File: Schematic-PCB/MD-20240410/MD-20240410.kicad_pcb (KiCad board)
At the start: 2 copper layers, 100.5 x 56.4 mm, 0 parts

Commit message: MD基板へ部品を仮で配置
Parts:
- added C1: 22n, Capacitor_SMD:C_0603_1608Metric, F.Cu at (147.8, 76.2)
- added C10: 220n, Capacitor_SMD:C_0603_1608Metric, F.Cu at (152.0, 76.2)
- added C11: 22n, Capacitor_SMD:C_0603_1608Metric, F.Cu at (147.8, 96.0)
- added C12: 220n, Capacitor_SMD:C_0603_1608Metric, F.Cu at (147.8, 99.0)
- added C13: 22n, Capacitor_SMD:C_0603_1608Metric, F.Cu at (152.2, 99.0)
- added C14: 220n, Capacitor_SMD:C_0603_1608Metric, F.Cu at (152.2, 96.0)
- added C2: 220n, Capacitor_SMD:C_0603_1608Metric, F.Cu at (147.8, 79.2)
- added C3: 4.7u, Capacitor_SMD:C_0603_1608Metric, F.Cu at (153.5, 87.5)
- added C4: 4.7u, Capacitor_SMD:C_0603_1608Metric, F.Cu at (155.0, 87.5)
- added C5: 50u, Capacitor_SMD:C_0603_1608Metric, F.Cu at (156.5, 87.5)
- added C7: 0.1u, Capacitor_SMD:C_0603_1608Metric, F.Cu at (158.0, 87.5)
- added C8: 0.1u, Capacitor_SMD:C_0603_1608Metric, F.Cu at (159.5, 87.5)
- added C9: 22n, Capacitor_SMD:C_0603_1608Metric, F.Cu at (152.0, 79.2)
- added D1: LED, LED_SMD:LED_0805_2012Metric, B.Cu at (168.5, 87.5)
- added D2: 16.2V, Diode_SMD:D_SOD-323, F.Cu at (136.8, 87.5)
- added J1: Conn_01x05_Pin, Connector_FFC-FPC:TE_84953-5_1x05-1MP_P1.0mm_Horizontal, F.Cu at (120.8, 87.5)
- added J2: Conn_01x05_Pin, Connector_FFC-FPC:TE_84953-5_1x05-1MP_P1.0mm_Horizontal, F.Cu at (179.2, 87.5)
- added J3: Conn_01x02_Pin, Connector_JST:JST_VH_B2P-VH_1x02_P3.96mm_Vertical, F.Cu at (130.8, 75.5)
- added J4: Conn_01x02_Pin, Connector_JST:JST_VH_B2P-VH_1x02_P3.96mm_Vertical, F.Cu at (169.0, 79.5)
- added J5: Conn_01x02_Pin, Connector_JST:JST_VH_B2P-VH_1x02_P3.96mm_Vertical, F.Cu at (130.8, 95.5)
- added J6: Conn_01x02_Pin, Connector_JST:JST_VH_B2P-VH_1x02_P3.96mm_Vertical, F.Cu at (169.2, 99.5)
- added J7: Conn_01x02_Pin, Connector_JST:JST_VH_B2P-VH_1x02_P3.96mm_Vertical, F.Cu at (130.8, 85.5)
- added Q2: PMOS, Package_TO_SOT_SMD:TO-252-2, F.Cu at (145.0, 87.5)
- added R1: 330, Resistor_SMD:R_0603_1608Metric, F.Cu at (165.8, 87.5)
- added R10: NP, Resistor_SMD:R_0603_1608Metric, F.Cu at (163.0, 78.5)
- added R11: 20k, Resistor_SMD:R_0603_1608Metric, F.Cu at (163.0, 75.5)
- added R12: 2.49k, Resistor_SMD:R_0603_1608Metric, F.Cu at (136.8, 98.2)
- added R13: 10k, Resistor_SMD:R_0603_1608Metric, F.Cu at (136.8, 95.2)
- added R14: NP, Resistor_SMD:R_0603_1608Metric, F.Cu at (136.8, 96.8)
- added R15: 20k, Resistor_SMD:R_0603_1608Metric, F.Cu at (136.8, 99.8)
- added R16: 2.49k, Resistor_SMD:R_0603_1608Metric, F.Cu at (163.2, 96.8)
- added R17: 10k, Resistor_SMD:R_0603_1608Metric, F.Cu at (163.2, 99.8)
- added R18: NP, Resistor_SMD:R_0603_1608Metric, F.Cu at (163.2, 98.2)
- added R19: 20k, Resistor_SMD:R_0603_1608Metric, F.Cu at (163.2, 95.2)
- added R3: 10k, Resistor_SMD:R_0603_1608Metric, F.Cu at (136.8, 75.5)
- added R4: 2.49k, Resistor_SMD:R_0603_1608Metric, F.Cu at (136.8, 78.5)
- added R5: 100k, Resistor_SMD:R_0603_1608Metric, F.Cu at (152.0, 87.5)
- added R6: NP, Resistor_SMD:R_0603_1608Metric, F.Cu at (136.8, 77.0)
- added R7: 20k, Resistor_SMD:R_0603_1608Metric, F.Cu at (136.8, 80.0)
- added R8: 2.49k, Resistor_SMD:R_0603_1608Metric, F.Cu at (163.0, 77.0)
- added R9: 10k, Resistor_SMD:R_0603_1608Metric, F.Cu at (163.0, 80.0)
- added U1: ~, Package_SO:HTSSOP-16-1EP_4.4x5mm_P0.65mm_EP3.4x5mm_Mask2.46x2.31mm_ThermalVias, F.Cu at (142.6, 77.7)
- added U2: ~, Package_SO:HTSSOP-16-1EP_4.4x5mm_P0.65mm_EP3.4x5mm_Mask2.46x2.31mm_ThermalVias, F.Cu at (157.1, 77.6)
- added U3: ~, Package_SO:HTSSOP-16-1EP_4.4x5mm_P0.65mm_EP3.4x5mm_Mask2.46x2.31mm_ThermalVias, F.Cu at (142.6, 97.5)
- added U4: ~, Package_SO:HTSSOP-16-1EP_4.4x5mm_P0.65mm_EP3.4x5mm_Mask2.46x2.31mm_ThermalVias, F.Cu at (157.4, 97.5)

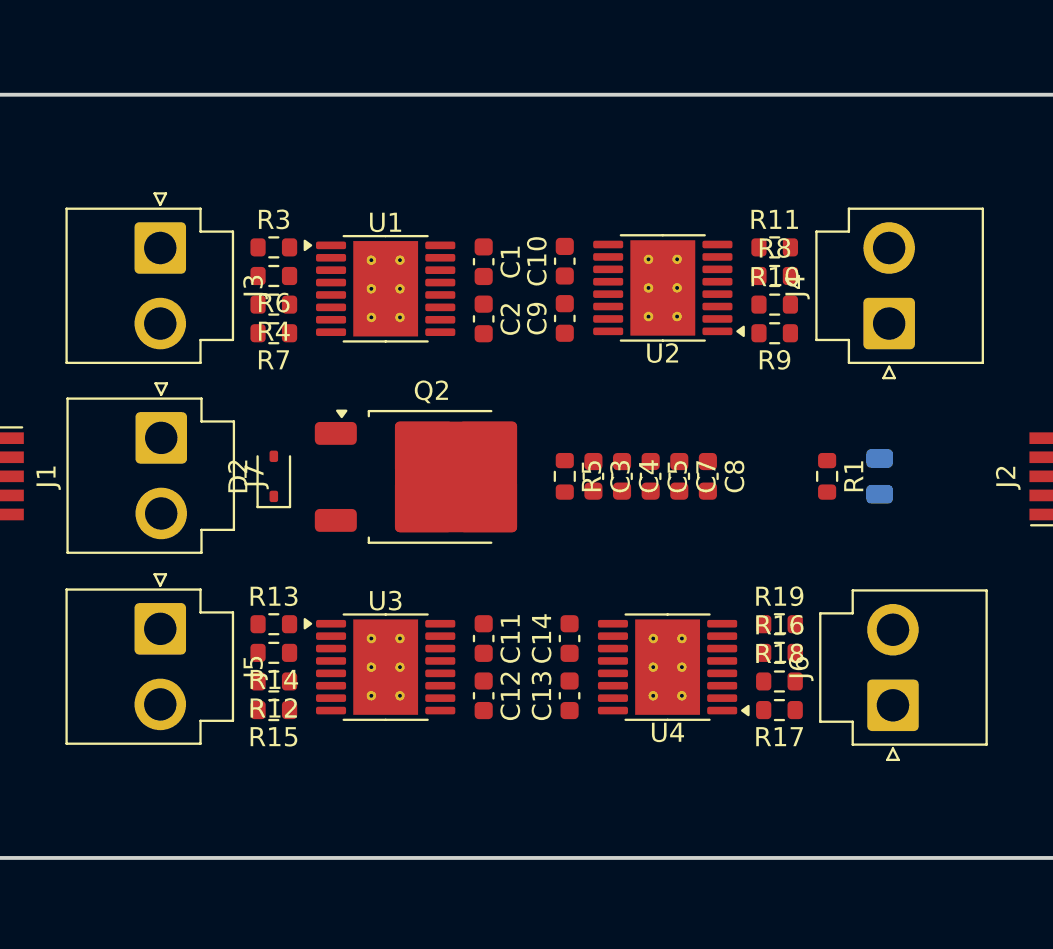
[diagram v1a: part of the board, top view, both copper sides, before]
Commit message: MD基板のPCBを更新
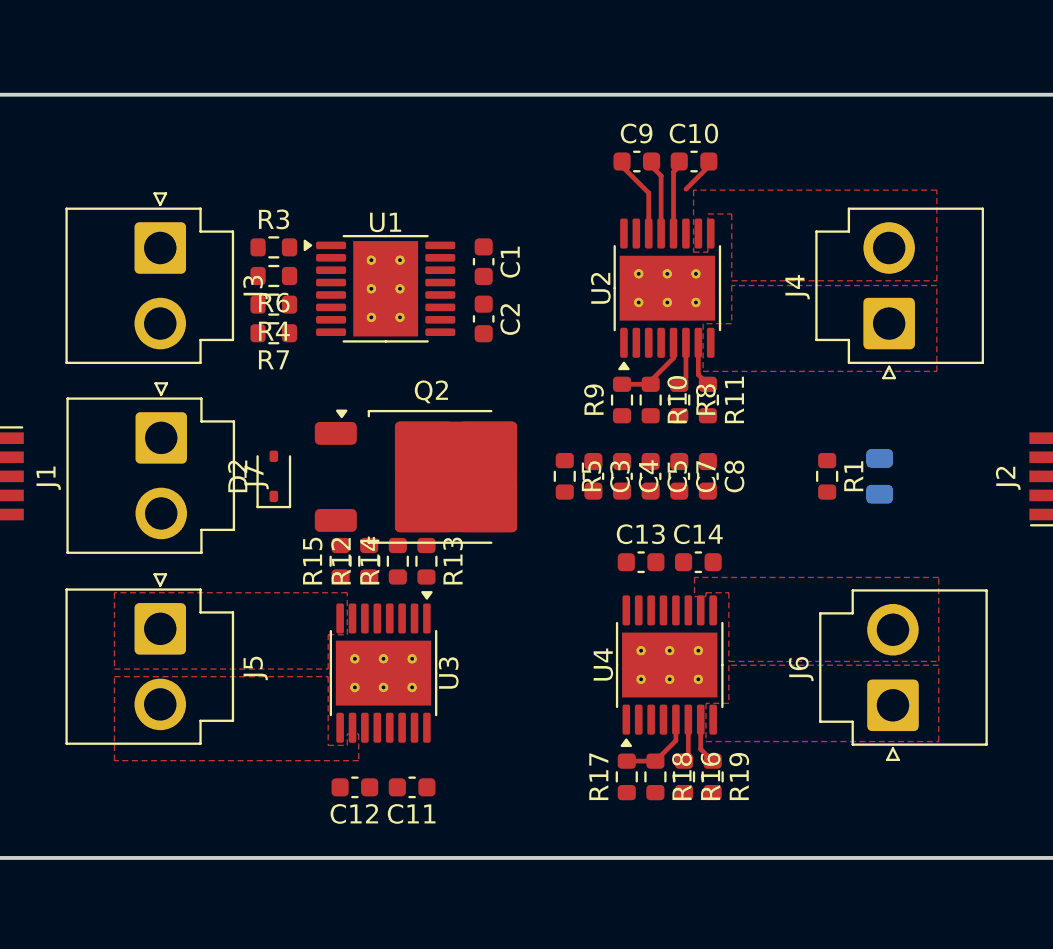
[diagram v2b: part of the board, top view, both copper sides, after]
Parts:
- moved C9 9.05 mm to (155.8, 71.0), turned to 0 degrees
- moved R11 8.73 mm to (159.5, 83.5), turned to -90 degrees
- moved R17 8.73 mm to (155.2, 103.2), turned to 90 degrees
- moved R19 8.73 mm to (159.8, 103.2), turned to -90 degrees
- moved R9 8.73 mm to (155.0, 83.5), turned to 90 degrees
- moved C11 8.65 mm to (144.0, 103.8), turned to 180 degrees
- moved R13 8.65 mm to (144.8, 92.0), turned to -90 degrees
- moved C10 8.56 mm to (158.8, 71.0), turned to 0 degrees
- moved R15 8.55 mm to (140.2, 92.0), turned to 90 degrees
- moved C12 8.28 mm to (141.0, 103.8), turned to 180 degrees
- moved R10 8.20 mm to (156.5, 83.5), turned to -90 degrees
- moved R16 8.20 mm to (158.2, 103.2), turned to -90 degrees
- moved R18 8.20 mm to (156.8, 103.2), turned to -90 degrees
- moved R8 8.20 mm to (158.0, 83.5), turned to -90 degrees
- moved R14 8.08 mm to (143.2, 92.0), turned to 90 degrees
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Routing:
- net VREF-2: track 0.00 -> 4.17 mm
- net VREF-4: track 0.00 -> 4.12 mm
- net Net-(U2-CPL): track 0.00 -> 4.10 mm
- net Net-(U2-CPH): track 0.00 -> 3.73 mm
- net Net-(U2-VCP): track 0.00 -> 3.65 mm
- net IMODE-4: track 0.00 -> 2.43 mm
- net IMODE-2: track 0.00 -> 2.38 mm
- net Net-(U2-IPROPI): track 0.00 -> 2.32 mm
- net Net-(U4-IPROPI): track 0.00 -> 2.27 mm
- net VM: track 0.00 -> 1.70 mm
- added copper zone on F.Cu, net OUT1-2
- added copper zone on F.Cu, net OUT1-3
- added copper zone on F.Cu, net OUT1-4
- added copper zone on F.Cu, net OUT2-2
- added copper zone on F.Cu, net OUT2-3
- added copper zone on F.Cu, net OUT2-4

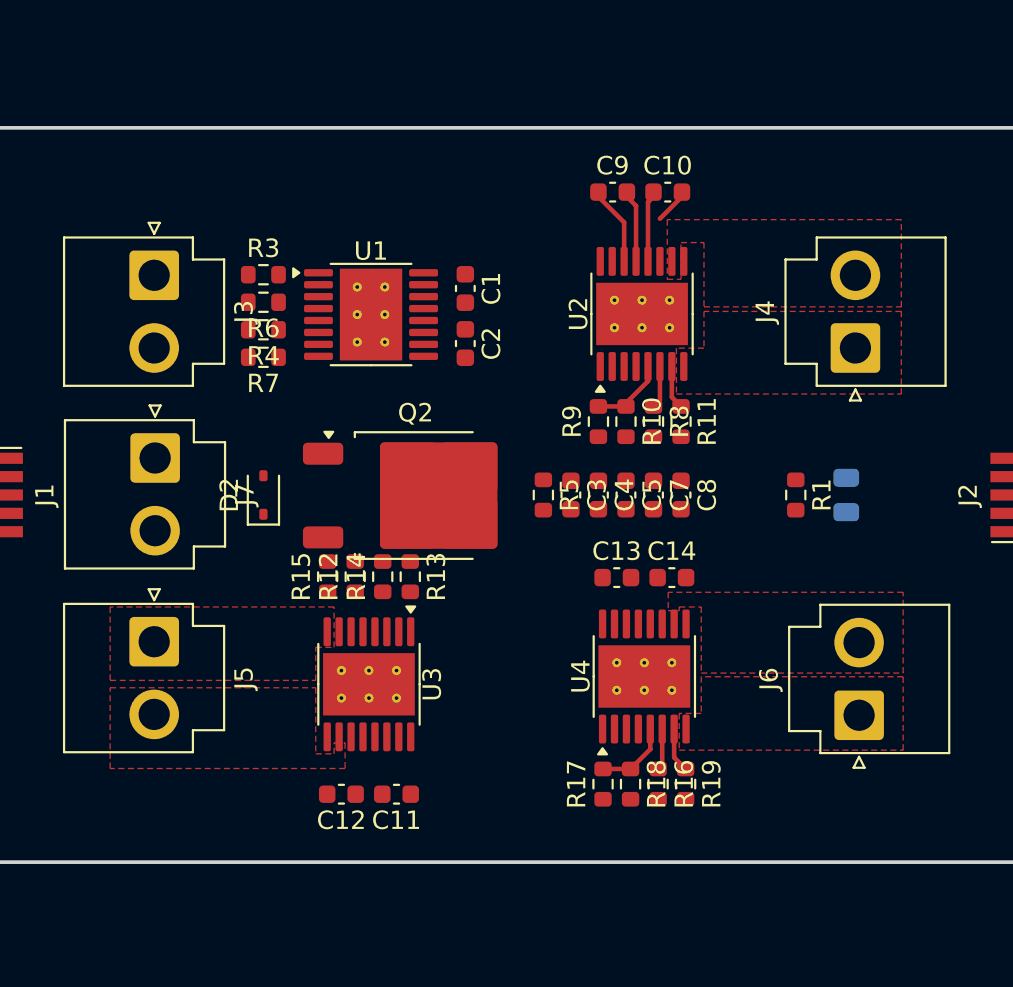
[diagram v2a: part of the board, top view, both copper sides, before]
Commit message: MD・ラインセンサの回路図を更新
メイン→ラインセンサ→MD と配線していたのを、
メイン→MD→ラインセンサ と経由するように変更した。

ラインセンサの回路図へ、コンパレータを使用するパターンの回路を追加で作成した。
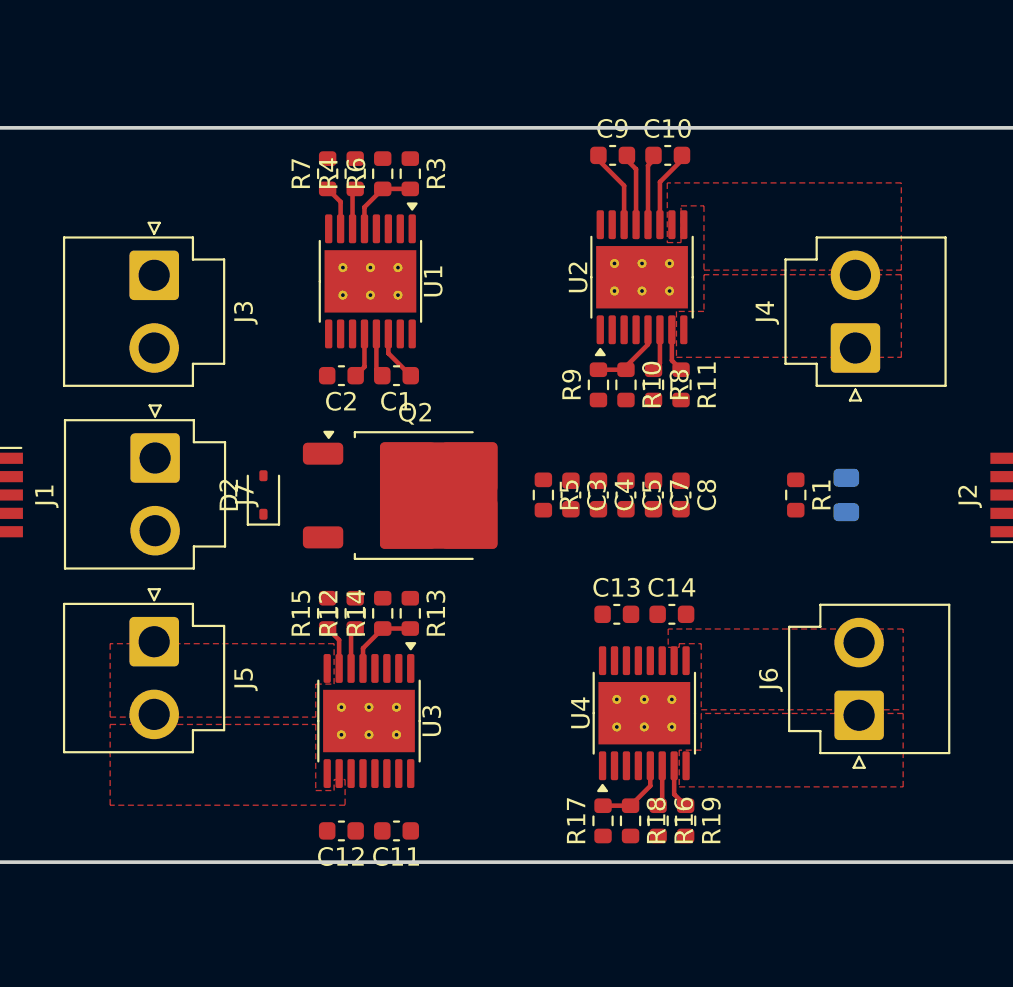
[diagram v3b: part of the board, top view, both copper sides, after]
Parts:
- moved R7 10.6 mm to (140.2, 70.0), turned to 90 degrees
- moved R4 9.86 mm to (141.8, 70.0), turned to 90 degrees
- moved R3 9.71 mm to (144.8, 70.0), turned to -90 degrees
- moved R6 9.55 mm to (143.2, 70.0), turned to 90 degrees
- moved C2 6.97 mm to (141.0, 81.0), turned to 180 degrees
- moved C1 6.05 mm to (144.0, 81.0), turned to 180 degrees
- moved C10 2.00 mm to (158.8, 69.0)
- moved C11 2.00 mm to (144.0, 105.8)
- moved C12 2.00 mm to (141.0, 105.8)
- moved C13 2.00 mm to (156.0, 94.0)
- moved C14 2.00 mm to (159.0, 94.0)
- moved C9 2.00 mm to (155.8, 69.0)
- moved R10 2.00 mm to (156.5, 81.5)
- moved R11 2.00 mm to (159.5, 81.5)
- moved R12 2.00 mm to (141.8, 94.0)
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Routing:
- net VREF-3: track 0.00 -> 4.12 mm
- net VREF-1: track 0.00 -> 4.09 mm
- net Net-(U1-CPL): track 0.00 -> 2.78 mm
- net Net-(U1-VCP): track 0.00 -> 2.47 mm
- net IMODE-1: track 0.00 -> 2.47 mm
- net IMODE-3: track 0.00 -> 2.43 mm
- net Net-(U1-CPH): track 0.00 -> 2.41 mm
- net VM: track 1.70 -> 4.02 mm
- net Net-(U3-IPROPI): track 0.00 -> 2.27 mm
- net Net-(U1-IPROPI): track 0.00 -> 2.24 mm

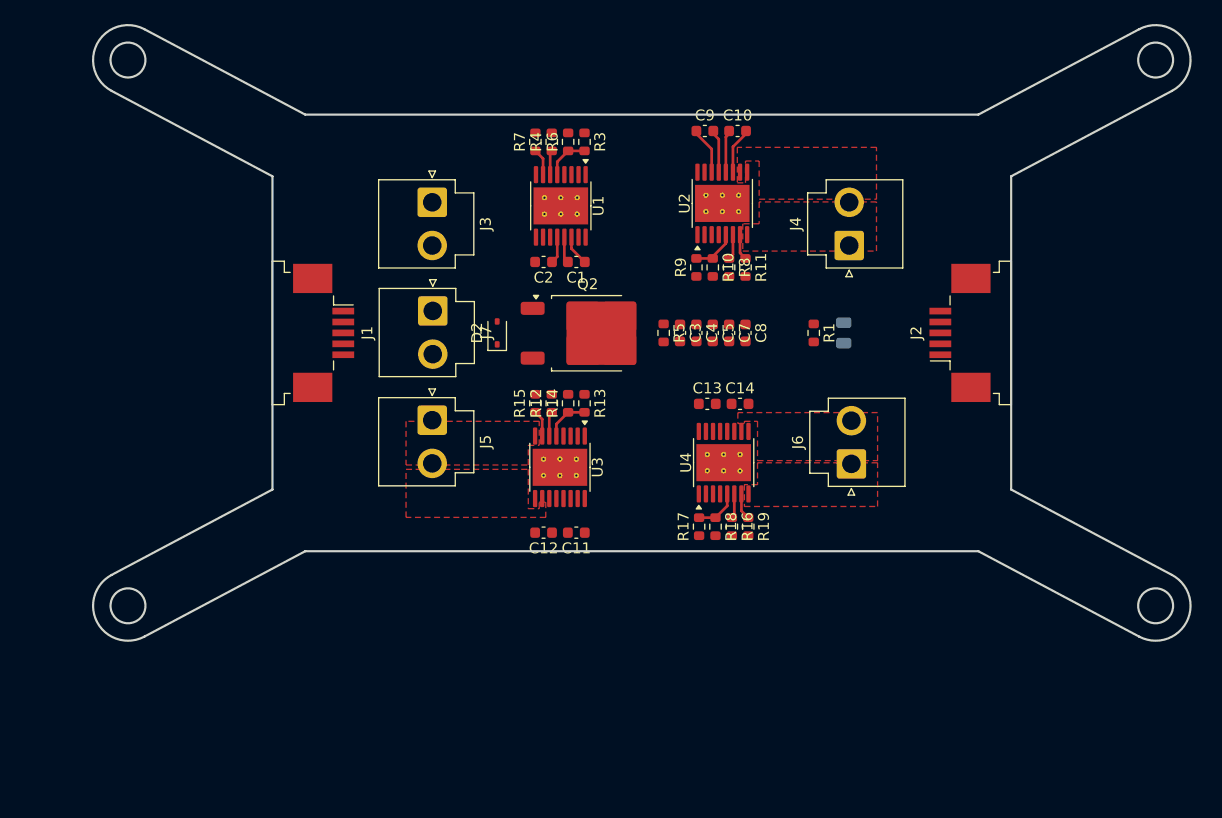
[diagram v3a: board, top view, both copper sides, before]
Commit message: キッカー・MD・ラインセンサ・電源基板を更新
キッカー :
・基板外形変更後のPCBの修正が途中で止まっていたため、残りの部分を編集した

ラインセンサ :
・以前のラインセンサ回路を、コンパレータを使用する回路へと置換した
・ラベル line_threshold を、PWM出力可能な5番ピンに設定した

MD :
・キッカーもMD基板を経由させるように変更した
・ラインセンサ用にレベル変換回路を作成した

電源基板 :
・フットプリントを一部指定した
・基板外形をインポートした
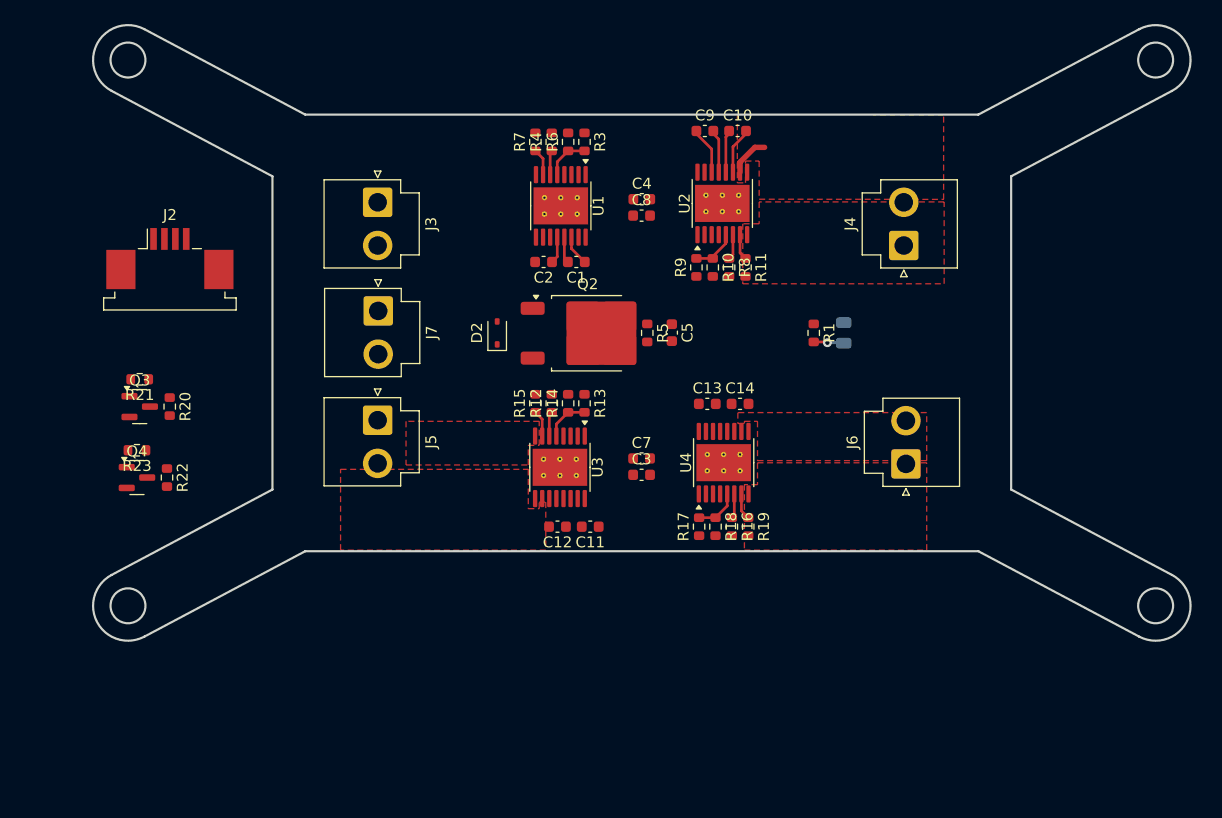
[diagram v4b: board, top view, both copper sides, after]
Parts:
- removed J1: Conn_01x05_Pin, Connector_FFC-FPC:TE_84953-5_1x05-1MP_P1.0mm_Horizontal
- added Q3: NMOS, Package_TO_SOT_SMD:SOT-23, F.Cu at (104.0, 94.2)
- added Q4: NMOS, Package_TO_SOT_SMD:SOT-23, F.Cu at (103.8, 100.8)
- added R20: 10k, Resistor_SMD:R_0603_1608Metric, F.Cu at (106.8, 94.2)
- added R21: 10k, Resistor_SMD:R_0603_1608Metric, F.Cu at (104.0, 91.8)
- added R22: 10k, Resistor_SMD:R_0603_1608Metric, F.Cu at (106.5, 100.8)
- added R23: 10k, Resistor_SMD:R_0603_1608Metric, F.Cu at (103.8, 98.2)
- J2: value Conn_01x05_Pin -> Conn_01x04_Pin; footprint Connector_FFC-FPC:TE_84953-5_1x05-1MP_P1.0mm_Horizontal -> Connector_FFC-FPC:TE_84953-4_1x04-1MP_P1.0mm_Horizontal
- moved J2 72.7 mm to (106.8, 80.7), turned to 0 degrees
- moved C8 14.4 mm to (150.0, 76.8), turned to 0 degrees
- moved C7 14.0 mm to (150.0, 99.0), turned to 0 degrees
- moved C3 13.5 mm to (150.0, 100.5), turned to 0 degrees
- moved C4 13.2 mm to (150.0, 75.2), turned to 0 degrees
- moved J3 5.00 mm to (125.8, 75.5)
- moved J5 5.00 mm to (125.8, 95.5)
- moved J4 5.00 mm to (174.0, 79.5)
- moved J6 5.00 mm to (174.2, 99.5)
- moved J7 5.00 mm to (125.8, 85.5)
- moved C5 3.75 mm to (152.8, 87.5)
- moved R5 1.50 mm to (150.5, 87.5)
- moved C11 1.39 mm to (145.3, 105.2)
- moved C12 1.39 mm to (142.3, 105.2)
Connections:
- J2 pad 1: EN-3 -> Line-MD-Main=RX_5V
- J2 pad 2: PH-3 -> Line-MD-Main=TX_5V
- J2 pad 3: EN-4 -> +5V
- J2 pad 4: PH-4 -> GND
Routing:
- net OUT2-2: track 0.00 -> 3.73 mm
- net Net-(D1-A): track 0.00 -> 2.80 mm, vias 0 -> 1
